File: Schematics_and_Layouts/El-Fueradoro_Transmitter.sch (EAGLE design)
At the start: 58 parts, among them IC1 MAX202, IC2 MEGA168P/328P, IC3 LM3940IT-3.3, Q1 9.8304

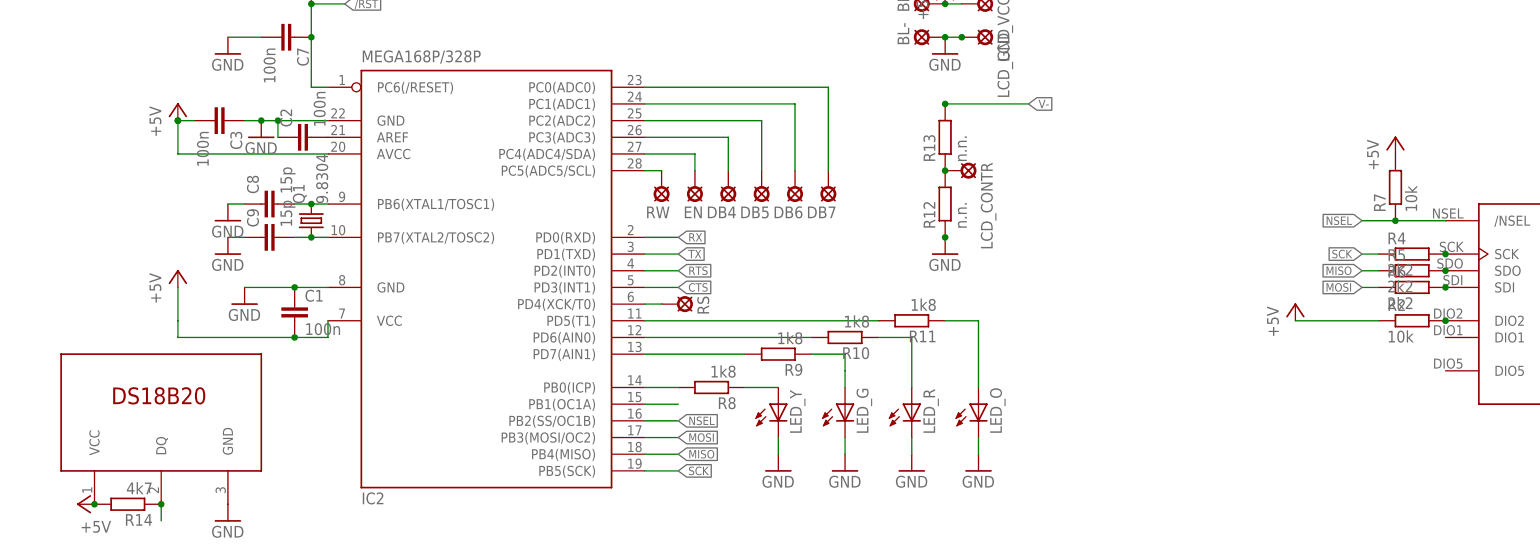
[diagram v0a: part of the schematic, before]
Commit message: Added bill of materials
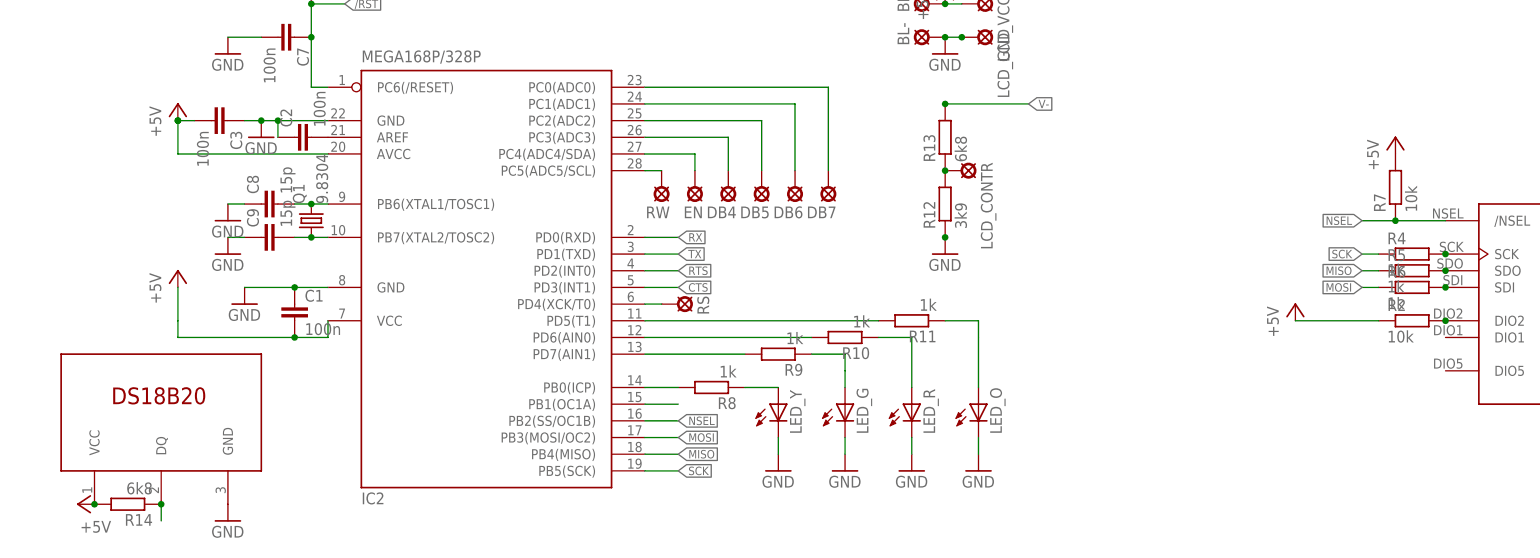
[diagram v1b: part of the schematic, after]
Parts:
- R10, R11, R8, R9: value 1k8 -> 1k
- R12: value n.n. -> 3k9
- R13: value n.n. -> 6k8
- R14: value 4k7 -> 6k8
- R4, R5, R6: value 2k2 -> 1k
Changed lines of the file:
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@@
 <part name="P+3" library="supply1" deviceset="+5V" device=""/>
 <part name="P+7" library="supply1" deviceset="+5V" device=""/>
-<part name="R4" library="rcl" deviceset="R-EU_" device="0207/10" value="2k2"/>
-<part name="R5" library="rcl" deviceset="R-EU_" device="0207/10" value="2k2"/>
-<part name="R6" library="rcl" deviceset="R-EU_" device="0207/10" value="2k2"/>
+<part name="R4" library="rcl" deviceset="R-EU_" device="0207/10" value="1k"/>
+<part name="R5" library="rcl" deviceset="R-EU_" device="0207/10" value="1k"/>
+<part name="R6" library="rcl" deviceset="R-EU_" device="0207/10" value="1k"/>
 <part name="GND6" library="supply1" deviceset="GND" device=""/>
 <part name="GND8" library="supply1" deviceset="GND" device=""/>
@@
 <part name="GND9" library="supply1" deviceset="GND" device=""/>
 <part name="GND10" library="supply1" deviceset="GND" device=""/>
-<part name="R8" library="rcl" deviceset="R-EU_" device="0207/10" value="1k8"/>
-<part name="R9" library="rcl" deviceset="R-EU_" device="0207/10" value="1k8"/>
-<part name="R10" library="rcl" deviceset="R-EU_" device="0207/10" value="1k8"/>
-<part name="R11" library="rcl" deviceset="R-EU_" device="0207/10" value="1k8"/>
+<part name="R8" library="rcl" deviceset="R-EU_" device="0207/10" value="1k"/>
+<part name="R9" library="rcl" deviceset="R-EU_" device="0207/10" value="1k"/>
+<part name="R10" library="rcl" deviceset="R-EU_" device="0207/10" value="1k"/>
+<part name="R11" library="rcl" deviceset="R-EU_" device="0207/10" value="1k"/>
 <part name="LED_O" library="led" deviceset="LED" device="5MM"/>
 <part name="LED_R" library="led" deviceset="LED" device="5MM"/>
@@
 <part name="DB7" library="solpad" deviceset="LSP10" device=""/>
 <part name="RS" library="solpad" deviceset="LSP10" device=""/>
-<part name="R12" library="rcl" deviceset="R-EU_" device="0207/10" value="n.n."/>
-<part name="R13" library="rcl" deviceset="R-EU_" device="0207/10" value="n.n."/>
+<part name="R12" library="rcl" deviceset="R-EU_" device="0207/10" value="3k9"/>
+<part name="R13" library="rcl" deviceset="R-EU_" device="0207/10" value="6k8"/>
 <part name="GND22" library="supply1" deviceset="GND" device=""/>
 <part name="LCD_VCC" library="solpad" deviceset="LSP10" device=""/>
@@
 <part name="U$2" library="fp" deviceset="DS18B20" device=""/>
 <part name="P+13" library="supply1" deviceset="+5V" device=""/>
-<part name="R14" library="rcl" deviceset="R-EU_" device="0207/10" value="4k7"/>
+<part name="R14" library="rcl" deviceset="R-EU_" device="0207/10" value="6k8"/>
 <part name="GND26" library="supply1" deviceset="GND" device=""/>
 <part name="U$3" library="fp" deviceset="RFM69CW" device=""/>

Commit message: Added size-information-output for Hexfiles/build_hexfiles.bat Extended manual and added BOMs BOM-Update (final one, hopefully!)
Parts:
- C14: value (none) -> 10u
- R12: value 3k9 -> 3k3
- R14: value 6k8 -> 3k3
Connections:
- net +5V renamed +3V3

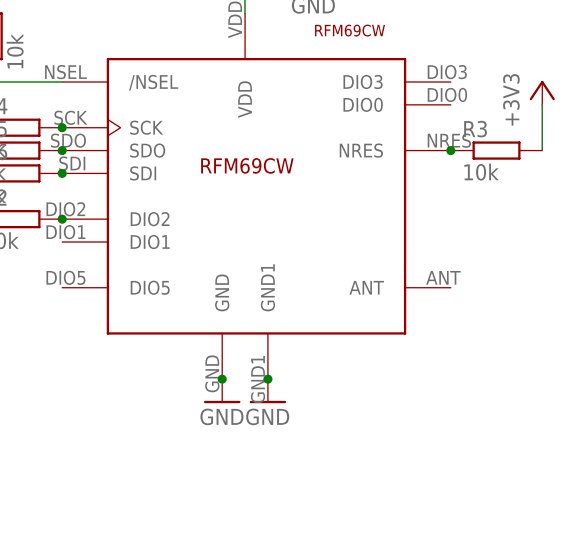
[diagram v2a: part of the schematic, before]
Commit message: Layout fixes Additions to manual once again
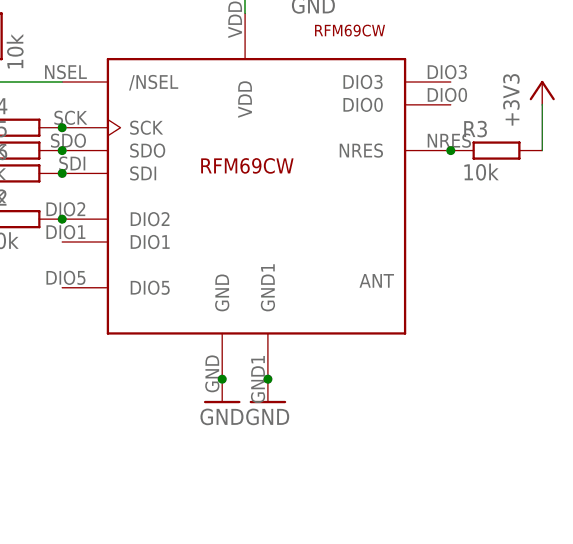
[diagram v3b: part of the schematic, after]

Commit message: Added Gerber Files
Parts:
- renumbered USB+ to +5V, USB+1 to D+, USB+2 to D-, USB- to GND
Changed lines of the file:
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@@
 <part name="SV2" library="fp" deviceset="ML10" device=""/>
 <part name="X1" library="fp" deviceset="F09HPS" device=""/>
-<part name="USB+" library="solpad" deviceset="LSP10" device=""/>
-<part name="USB-" library="solpad" deviceset="LSP10" device=""/>
-<part name="USB+1" library="solpad" deviceset="LSP10" device=""/>
-<part name="USB+2" library="solpad" deviceset="LSP10" device=""/>
+<part name="+5V" library="solpad" deviceset="LSP10" device=""/>
+<part name="GND" library="solpad" deviceset="LSP10" device=""/>
+<part name="D+" library="solpad" deviceset="LSP10" device=""/>
+<part name="D-" library="solpad" deviceset="LSP10" device=""/>
 <part name="GND15" library="supply1" deviceset="GND" device=""/>
 <part name="IC3" library="linear" deviceset="78*" device="TV" technology="6" value="LM3940IT-3.3"/>
@@
 <instance part="X1" gate="-7" x="256.54" y="101.6"/>
 <instance part="X1" gate="-8" x="256.54" y="106.68"/>
-<instance part="USB+" gate="1" x="5.08" y="132.08" rot="R90"/>
-<instance part="USB-" gate="1" x="5.08" y="124.46" rot="R90"/>
-<instance part="USB+1" gate="1" x="5.08" y="139.7" rot="R90"/>
-<instance part="USB+2" gate="1" x="7.62" y="142.24" rot="R90"/>
+<instance part="+5V" gate="1" x="5.08" y="132.08" rot="R90"/>
+<instance part="GND" gate="1" x="5.08" y="124.46" rot="R90"/>
+<instance part="D+" gate="1" x="5.08" y="139.7" rot="R90"/>
+<instance part="D-" gate="1" x="7.62" y="142.24" rot="R90"/>
 <instance part="GND15" gate="1" x="220.98" y="139.7"/>
 <instance part="IC3" gate="A1" x="35.56" y="132.08"/>
@@
 <pinref part="C11" gate="G$1" pin="-"/>
 <pinref part="GND17" gate="1" pin="GND"/>
-<pinref part="USB-" gate="1" pin="MP"/>
-<pinref part="USB-" gate="1" pin="MP"/>
+<pinref part="GND" gate="1" pin="MP"/>
+<pinref part="GND" gate="1" pin="MP"/>
 <junction x="7.62" y="124.46"/>
 </segment>
@@
 <wire x1="17.78" y1="132.08" x2="25.4" y2="132.08" width="0.1524" layer="91"/>
 <junction x="17.78" y="132.08"/>
-<pinref part="USB+" gate="1" pin="MP"/>
+<pinref part="+5V" gate="1" pin="MP"/>
 <junction x="7.62" y="132.08"/>
 </segment>
